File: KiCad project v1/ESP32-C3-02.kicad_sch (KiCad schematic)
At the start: 30 parts, among them J2 GSD090012SEU, U3 ESP32-C3-WROOM-02-H4, U4 CP2102N-Axx-xQFN20, U5 W25Q32JVSSIQ

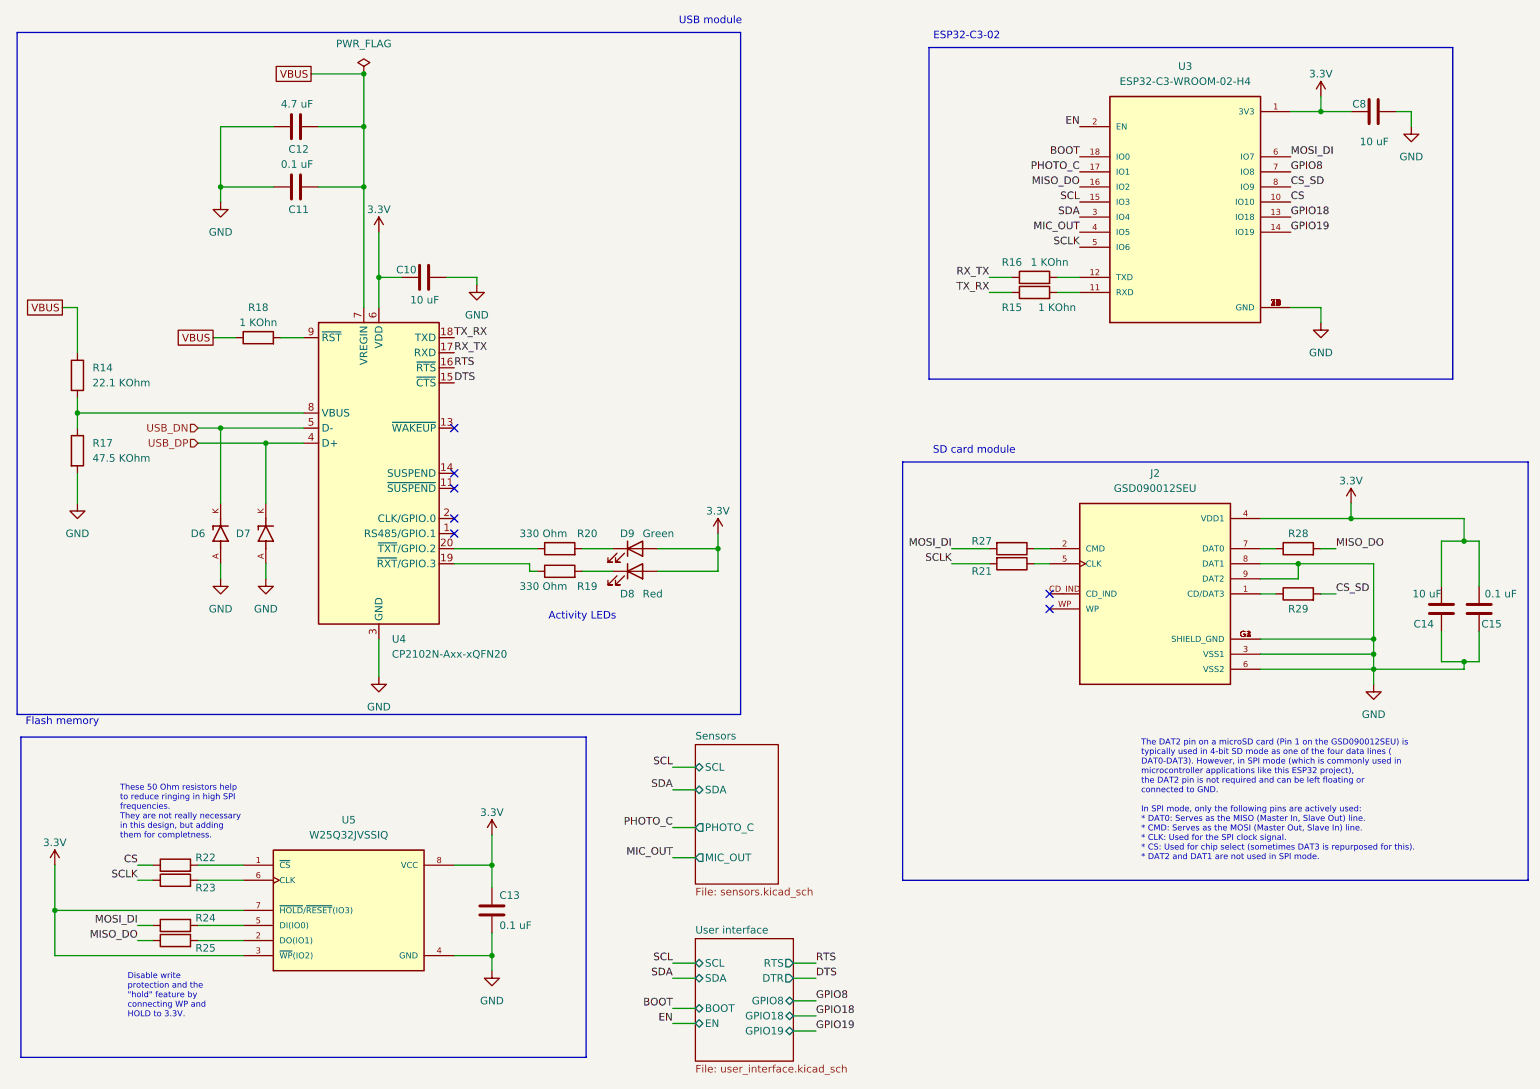
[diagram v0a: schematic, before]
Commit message: Simplifying component values by removing units.
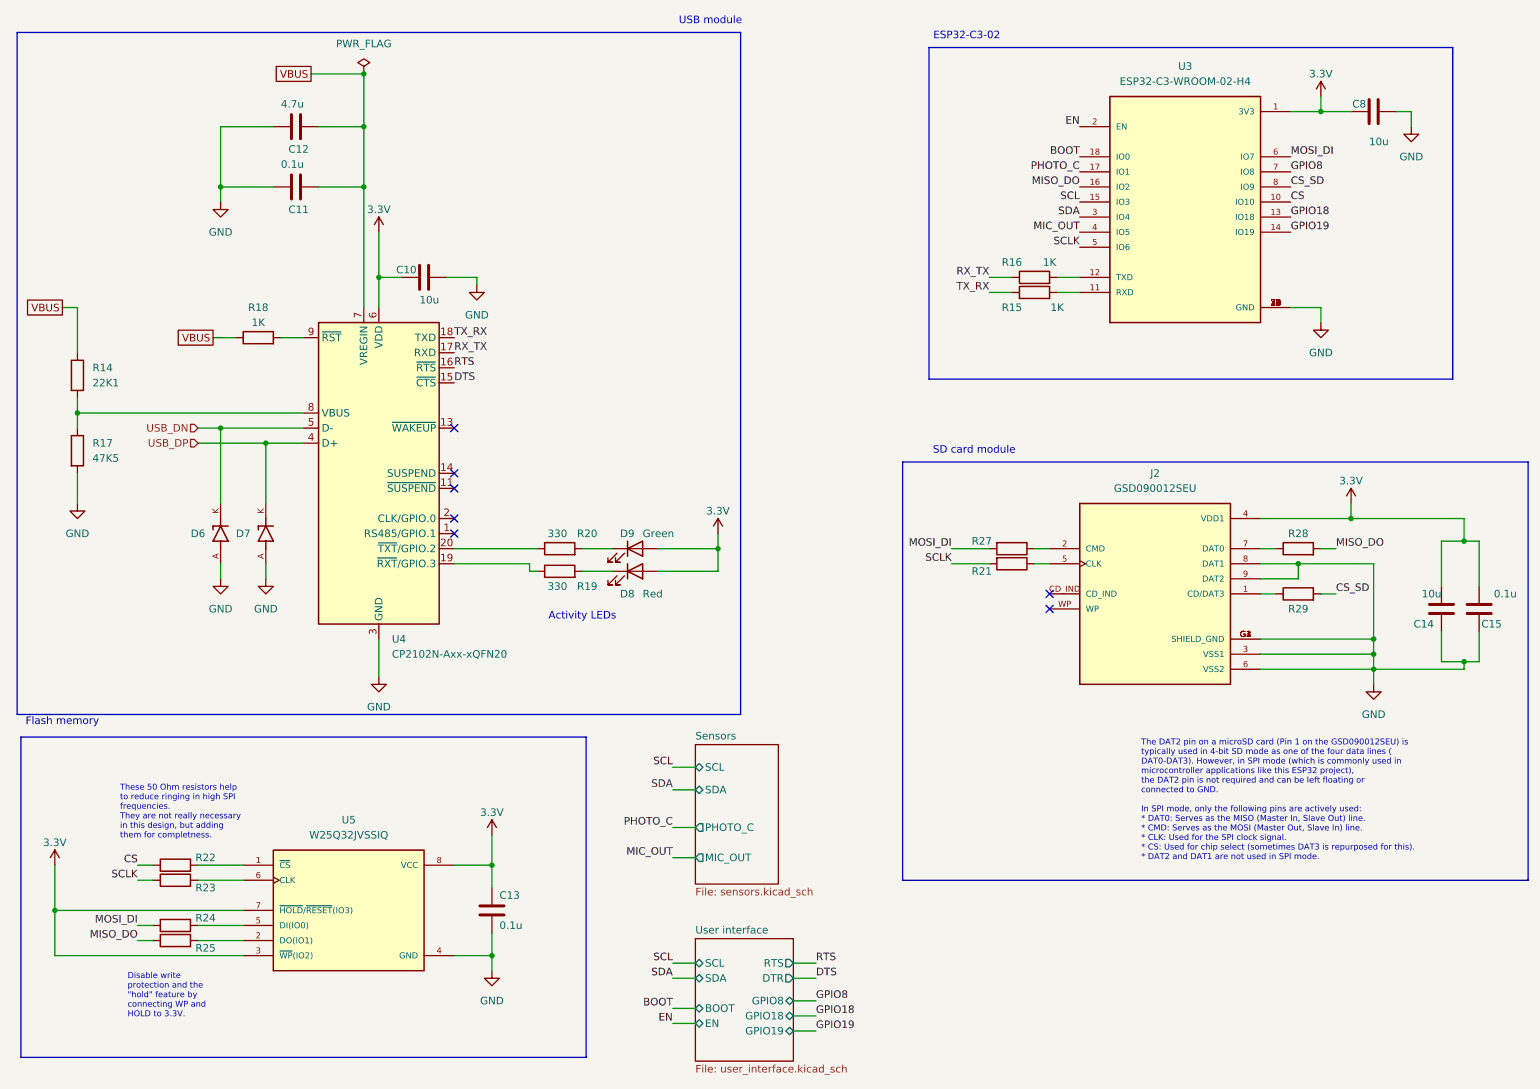
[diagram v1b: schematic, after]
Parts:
- C10, C14, C8: value 10 uF -> 10u
- C11, C13, C15: value 0.1 uF -> 0.1u
- C12: value 4.7 uF -> 4.7u
- R14: value 22.1 KOhm -> 22K1
- R15, R16, R18: value 1 KOhn -> 1K
- R17: value 47.5 KOhm -> 47K5
- R19, R20: value 330 Ohm -> 330
- R21, R22, R23, R24, R25, R27, R28, R29: value 50 Ohm -> 50
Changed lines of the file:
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@@
 			)
 		)
-		(property "Value" "50 Ohm"
+		(property "Value" "50"
 			(at 191.77 106.68 90)
 			(effects
@@
 			)
 		)
-		(property "Value" "50 Ohm"
+		(property "Value" "50"
 			(at 50.8 165.1 90)
 			(effects
@@
 			)
 		)
-		(property "Value" "50 Ohm"
+		(property "Value" "50"
 			(at 191.77 109.22 90)
 			(effects
@@
 			)
 		)
-		(property "Value" "50 Ohm"
+		(property "Value" "50"
 			(at 240.03 99.06 90)
 			(effects
@@
 			)
 		)
-		(property "Value" "22.1 KOhm"
+		(property "Value" "22K1"
 			(at 36.83 74.9299 0)
 			(effects
@@
 			)
 		)
-		(property "Value" "50 Ohm"
+		(property "Value" "50"
 			(at 50.8 152.4 90)
 			(effects
@@
 			)
 		)
-		(property "Value" "50 Ohm"
+		(property "Value" "50"
 			(at 50.8 154.94 90)
 			(effects
@@
 			)
 		)
-		(property "Value" "10 uF"
+		(property "Value" "10u"
 			(at 255.27 34.29 90)
 			(effects
@@
 			)
 		)
-		(property "Value" "1 KOhn"
+		(property "Value" "1K"
 			(at 199.39 62.23 90)
 			(effects
@@
 			)
 		)
-		(property "Value" "4.7 uF"
+		(property "Value" "4.7u"
 			(at 68.58 27.94 90)
 			(effects
@@
 			)
 		)
-		(property "Value" "1 KOhn"
+		(property "Value" "1K"
 			(at 198.12 54.61 90)
 			(effects
@@
 			)
 		)
-		(property "Value" "47.5 KOhm"
+		(property "Value" "47K5"
 			(at 36.83 87.6299 0)
 			(effects
@@
 			)
 		)
-		(property "Value" "330 Ohm"
+		(property "Value" "330"
 			(at 116.84 100.33 90)
 			(effects
@@
 			)
 		)
-		(property "Value" "0.1 uF"
+		(property "Value" "0.1u"
 			(at 276.86 110.49 0)
 			(effects
@@
 			)
 		)
-		(property "Value" "10 uF"
+		(property "Value" "10u"
 			(at 264.16 110.49 0)
 			(effects
@@
 			)
 		)
-		(property "Value" "330 Ohm"
+		(property "Value" "330"
 			(at 116.84 109.22 90)
 			(effects
@@
 			)
 		)
-		(property "Value" "0.1 uF"
+		(property "Value" "0.1u"
 			(at 68.58 38.1 90)
 			(effects
@@
 			)
 		)
-		(property "Value" "50 Ohm"
+		(property "Value" "50"
 			(at 50.8 162.56 90)
 			(effects
@@
 			)
 		)
-		(property "Value" "10 uF"
+		(property "Value" "10u"
 			(at 95.25 60.96 90)
 			(effects
@@
 			)
 		)
-		(property "Value" "1 KOhn"
+		(property "Value" "1K"
 			(at 64.77 64.77 90)
 			(effects
@@
 			)
 		)
-		(property "Value" "50 Ohm"
+		(property "Value" "50"
 			(at 240.03 106.68 90)
 			(effects
@@
 			)
 		)
-		(property "Value" "0.1 uF"
+		(property "Value" "0.1u"
 			(at 105.41 166.37 0)
 			(effects
